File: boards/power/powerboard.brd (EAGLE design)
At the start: 83 x 42 mm, 42 parts, among them IC1 TPS5420, IC2 TPS5420

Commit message: finished powerboard changes
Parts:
- moved R4 11.2 mm to (43.5, 36.2)
- moved R1 7.13 mm to (33.6, 38.2)
- moved R7 3.36 mm to (39.5, 36.2), turned to 180 degrees
- moved R2 1.55 mm to (6.17, 8.89)
- moved U$1 1.52 mm to (51.8, 33.4)
- moved R3 1.05 mm to (5.48, 17.4)
- moved R6 1.05 mm to (5.56, 13.2)
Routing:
- net 5V: track 23.2 -> 35.5 mm
- net N$6: track 27.0 -> 34.5 mm
- net GND: track 0.37 -> 7.49 mm, vias 5 -> 6
- net N$5: track 2.56 -> 9.58 mm
- net N$12: track 30.5 -> 24.7 mm, vias 3 -> 2
- net N$19: track 1.16 -> 2.76 mm
- net N$18: track 5.03 -> 4.28 mm

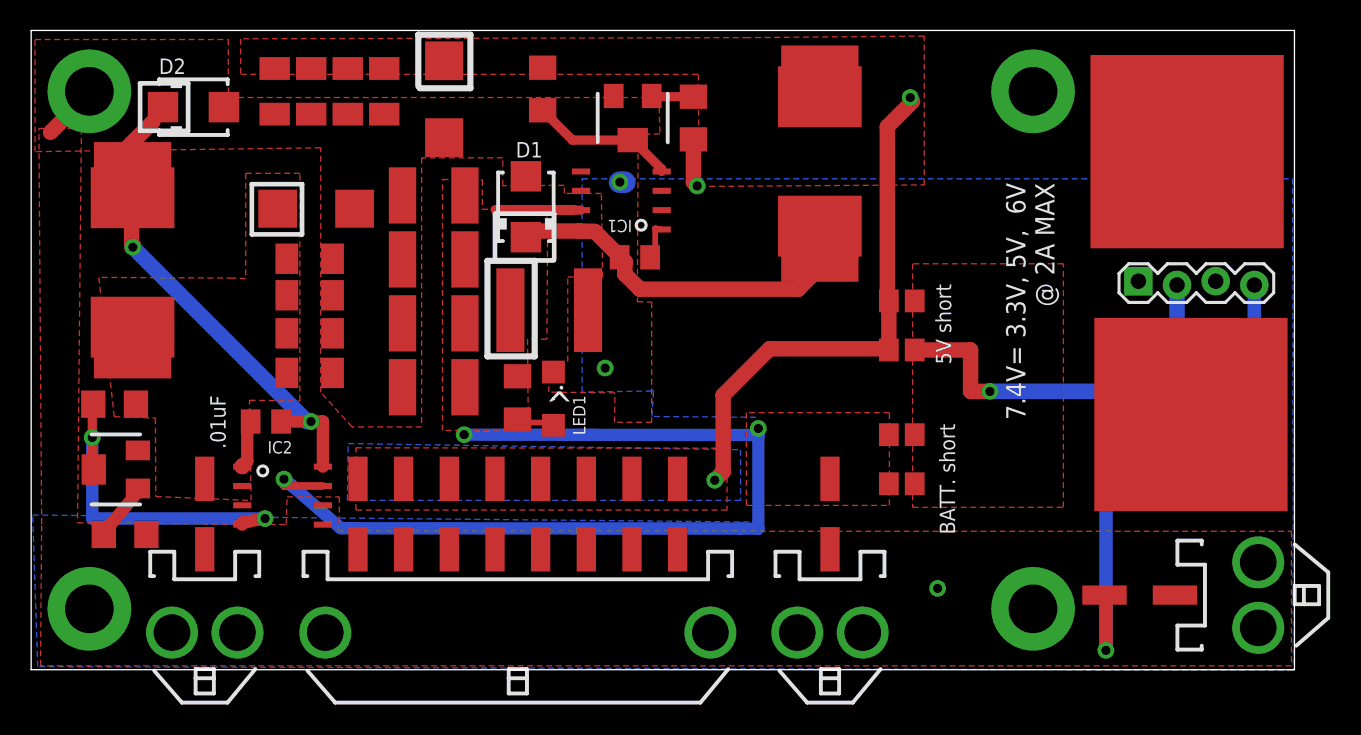
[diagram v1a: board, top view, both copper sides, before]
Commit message: changed resistors and fixed text
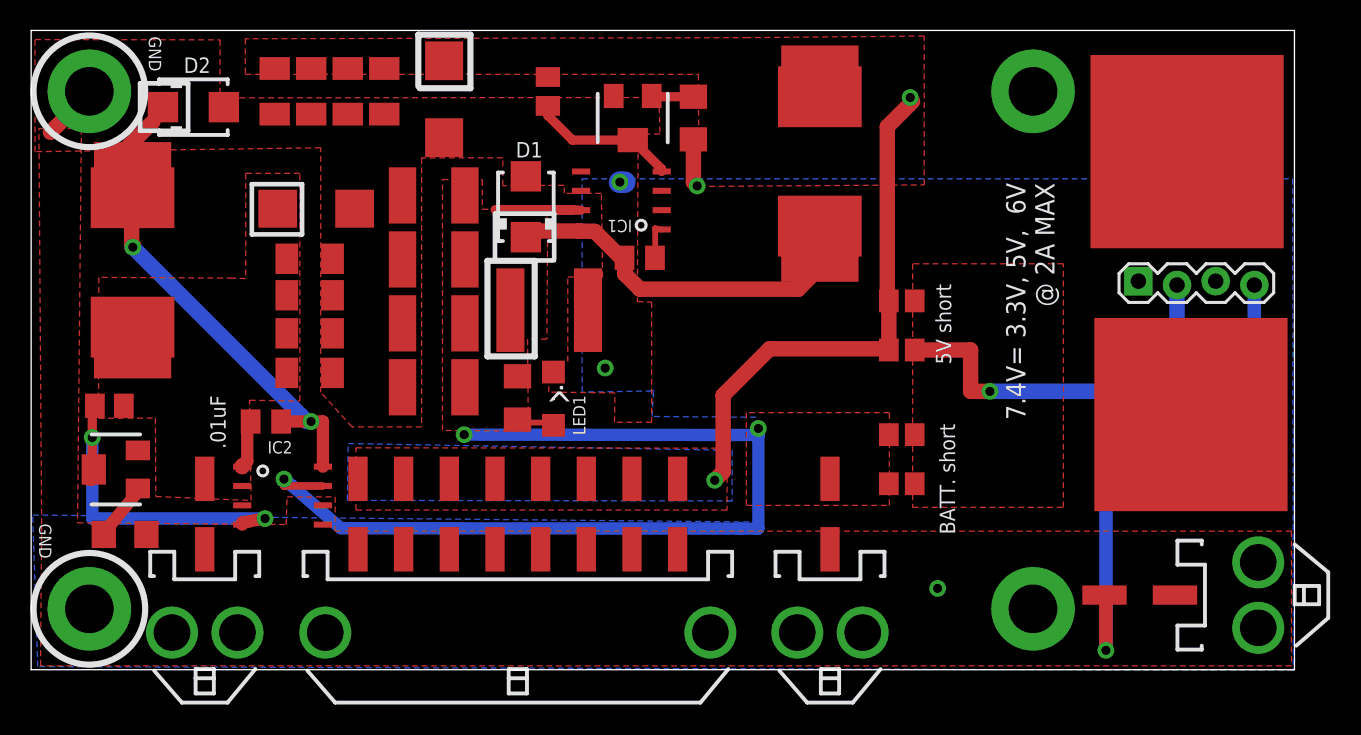
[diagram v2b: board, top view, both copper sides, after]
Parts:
- removed R1, R3: 10.0k, rcl:R3216
- added R12, R13: 10k, rcl:M0805
- R2, R4: value 500 -> 470
- moved C8 0.32 mm to (40.0, 27.1)
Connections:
- net 3_3V: now also R13.2; no longer R3.2
- net 5V: now also R12.2; no longer R1.2
- net N$12: now also R13.1; no longer R3.1
- net N$5: now also R12.1; no longer R1.1
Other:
- board text added: "GND"
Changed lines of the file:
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@@
 <setting verticaltext="up"/>
 </settings>
-<grid distance="0.01" unitdist="inch" unit="inch" style="lines" multiple="65" display="yes" altdistance="0.025" altunitdist="inch" altunit="inch"/>
+<grid distance="0.01" unitdist="mm" unit="mm" style="lines" multiple="65" display="yes" altdistance="0.025" altunitdist="inch" altunit="inch"/>
 <layers>
 <layer number="1" name="Top" color="4" fill="1" visible="yes" active="yes"/>
@@
 <text x="60.706" y="8.89" size="1.016" layer="25" font="vector" rot="R90">BATT. short</text>
 <text x="33.782" y="16.51" size="1.778" layer="25">^</text>
+<circle x="3.8246" y="4" radius="3.668" width="0.4064" layer="21"/>
+<text x="0.52" y="9.6" size="0.8128" layer="21" rot="SR270">GND</text>
+<text x="7.73" y="41.61" size="0.8128" layer="21" rot="SR270">GND</text>
+<circle x="3.8246" y="38" radius="3.668" width="0.4064" layer="21"/>
 </plain>
 <attributes>
@@
 <attribute name="NAME" x="33.6002" y="34.6696" size="1.016" layer="25" ratio="10" rot="R180"/>
 </element>
-<element name="C8" library="rcl" package="C0805K" value=".01uF" x="39.6642" y="27.094" smashed="yes">
-<attribute name="VALUE" x="38.9182" y="24.94" size="1.016" layer="27"/>
-</element>
-<element name="R1" library="rcl" package="R3216" value="10.0k" x="33.6074" y="38.154" smashed="yes" rot="R90">
-<attribute name="VALUE" x="35.8934" y="35.995" size="1.016" layer="27" rot="R90"/>
+<element name="C8" library="rcl" package="C0805K" value=".01uF" x="39.9842" y="27.064" smashed="yes">
+<attribute name="VALUE" x="39.2382" y="24.91" size="1.016" layer="27"/>
 </element>
 <element name="U$1" library="inductor-coilcraft-3" package="MSS1260" value="33uH" x="51.8188" y="33.3946" smashed="yes" rot="R180">
@@
 </element>
 <element name="D2" library="diode" package="SMA" value="MBRA340T3" x="10.662" y="36.9598" smashed="yes">
-<attribute name="NAME" x="8.3946" y="39.1376" size="1.016" layer="25" ratio="10"/>
+<attribute name="NAME" x="10.0246" y="39.2076" size="1.016" layer="25" ratio="10"/>
 </element>
 <element name="C17" library="rcl" package="C0805K" value=".01uF" x="15.4222" y="16.3056" smashed="yes" rot="R180">
 <attribute name="VALUE" x="11.7664" y="18.0224" size="1.016" layer="25" rot="R270"/>
-</element>
-<element name="R3" library="rcl" package="R3216" value="10.0k" x="5.4844" y="17.445" smashed="yes">
-<attribute name="VALUE" x="2.621" y="15.2634" size="1.016" layer="27" rot="R90"/>
 </element>
 <element name="U$3" library="inductor-coilcraft-3" package="MSS1260" value="33uH" x="6.6634" y="26.7566" smashed="yes">
@@
 <attribute name="VALUE" x="35.6624" y="38.5008" size="1.27" layer="27" rot="R270"/>
 </element>
-<element name="R2" library="rcl" package="R3216" value="500" x="6.1722" y="8.89" smashed="yes" rot="R180">
-<attribute name="VALUE" x="2.286" y="9.8552" size="1.016" layer="27" rot="R270"/>
-</element>
-<element name="R4" library="rcl" package="R3216" value="500" x="43.5102" y="36.2458" smashed="yes" rot="R90">
+<element name="R2" library="rcl" package="R3216" value="470" x="6.1722" y="8.89" smashed="yes" rot="R180">
+<attribute name="VALUE" x="2.226" y="10.5152" size="1.016" layer="27" rot="R270"/>
+</element>
+<element name="R4" library="rcl" package="R3216" value="470" x="43.5102" y="36.2458" smashed="yes" rot="R90">
 <attribute name="VALUE" x="44.9072" y="39.9542" size="1.016" layer="27" rot="R180"/>
 </element>
@@
 <attribute name="VALUE" x="31.236" y="19.647" size="1.016" layer="27"/>
 </element>
+<element name="R12" library="rcl" package="M0805" value="10k" x="33.95" y="37.99" smashed="yes" rot="R90">
+<attribute name="VALUE" x="32.43" y="36.18" size="1.27" layer="27" rot="R90"/>
+</element>
+<element name="R13" library="rcl" package="M0805" value="10k" x="5.14" y="17.34" smashed="yes">
+<attribute name="VALUE" x="7.27" y="16.79" size="1.27" layer="27"/>
+</element>
 </elements>
 <signals>
 <signal name="5V" class="1">
-<contactref element="R1" pad="2"/>
 <contactref element="C5" pad="1"/>
 <contactref element="C4" pad="1"/>
@@
 <polygon width="0.508" layer="1" isolate="0.8128">
 <vertex x="47.117" y="41.529"/>
-<vertex x="13.7668" y="41.4528"/>
-<vertex x="13.7668" y="39.116"/>
+<vertex x="14.0668" y="41.4528"/>
+<vertex x="14.0668" y="39.116"/>
 <vertex x="43.8404" y="39.116"/>
 <vertex x="43.8404" y="37.4142"/>
@@
 <vertex x="20.7746" y="11.1252"/>
 <vertex x="20.828" y="14.859"/>
-<vertex x="46.609" y="14.4526"/>
-<vertex x="46.609" y="11.1252"/>
+<vertex x="46.059" y="14.4126"/>
+<vertex x="46.059" y="11.0852"/>
 </polygon>
 <contactref element="X1" pad="P$9"/>
@@
 <wire x1="56.3508" y1="21.0058" x2="56.3118" y2="21.0058" width="1.016" layer="1"/>
 <wire x1="56.3118" y1="21.0058" x2="56.261" y2="20.955" width="1.016" layer="1"/>
+<contactref element="R12" pad="2"/>
 </signal>
 <signal name="N$2">
@@
 <wire x1="41" y1="27" x2="41" y2="29" width="0.381" layer="1"/>
 <wire x1="41" y1="29" x2="41.428" y2="28.924" width="0.381" layer="1"/>
-<wire x1="41" y1="27" x2="40.6642" y2="27.094" width="0.381" layer="1"/>
+<wire x1="41" y1="27" x2="40.9842" y2="27.064" width="0.381" layer="1"/>
 </signal>
 <signal name="N$5">
-<contactref element="R1" pad="1"/>
 <contactref element="IC1" pad="4"/>
 <contactref element="R7" pad="2"/>
-<wire x1="33.6074" y1="36.754" x2="35.5656" y2="34.7958" width="0.6096" layer="1"/>
 <wire x1="35.5656" y1="34.7958" x2="39.5224" y2="34.7958" width="0.6096" layer="1"/>
 <wire x1="39.5224" y1="34.7958" x2="41.428" y2="32.8902" width="0.6096" layer="1"/>
 <wire x1="41.428" y1="32.8902" x2="41.428" y2="32.734" width="0.6096" layer="1"/>
+<contactref element="R12" pad="1"/>
+<wire x1="35.5656" y1="34.7958" x2="33.95" y2="36.4114" width="0.6096" layer="1"/>
+<wire x1="33.95" y1="36.4114" x2="33.95" y2="37.04" width="0.6096" layer="1"/>
 </signal>
 <signal name="GND" class="1">
@@
 <vertex x="0.254" y="34.036"/>
 <vertex x="0.254" y="41.402"/>
-<vertex x="12.954" y="41.402"/>
-<vertex x="12.954" y="37.592"/>
+<vertex x="12.414" y="41.382"/>
+<vertex x="12.414" y="37.572"/>
 <vertex x="41.2412" y="37.592"/>
 <vertex x="41.3174" y="35.2044"/>
@@
 <vertex x="16.7522" y="9.5386"/>
 <vertex x="16.8148" y="11.3538"/>
-<vertex x="20.2438" y="11.3538"/>
-<vertex x="20.2438" y="9.9822"/>
-<vertex x="20.1168" y="9.0932"/>
-<vertex x="82.804" y="9.0932"/>
+<vertex x="19.9738" y="11.3538"/>
+<vertex x="19.9738" y="9.1032"/>
+<vertex x="82.804" y="9.1032"/>
 </polygon>
 <contactref element="LED1" pad="C"/>
@@
 <wire x1="40" y1="25" x2="39" y2="26" width="1.016" layer="1"/>
 <wire x1="50.4" y1="25" x2="40" y2="25" width="1.016" layer="1"/>
-<wire x1="39.0254" y1="26.7968" x2="38.6642" y2="27.094" width="0.381" layer="1"/>
+<wire x1="39.0254" y1="26.7968" x2="38.9842" y2="27.064" width="0.381" layer="1"/>
 <wire x1="49.631965625" y1="28.23630625" x2="51.8188" y2="29.1446" width="0.381" layer="1"/>
 <wire x1="50.4" y1="25" x2="52.832" y2="27.432" width="1.016" layer="1"/>
@@
 </signal>
 <signal name="3_3V" class="1">
-<contactref element="R3" pad="2"/>
 <contactref element="C14" pad="1"/>
 <contactref element="C13" pad="1"/>
@@
 <contactref element="X2" pad="P$2"/>
 <polygon width="0.508" layer="1">
-<vertex x="5.461" y="16.6174"/>
+<vertex x="4.431" y="16.5174"/>
 <vertex x="8.163" y="16.5354"/>
 <vertex x="8.1884" y="11.3782"/>
@@
 <vertex x="4.445" y="25.7744"/>
 </polygon>
+<contactref element="R13" pad="2"/>
 </signal>
 <signal name="N$10">
@@
 </signal>
 <signal name="N$12">
-<contactref element="R3" pad="1"/>
 <contactref element="IC2" pad="4"/>
 <contactref element="R6" pad="2"/>
 <wire x1="4.016" y1="13.254" x2="4.016" y2="15.254" width="0.6096" layer="1"/>
 <wire x1="4.016" y1="15.254" x2="4.016" y2="17.254" width="0.6096" layer="1"/>
-<wire x1="4.016" y1="17.254" x2="4.0844" y2="17.445" width="0.381" layer="1"/>
 <wire x1="4.016" y1="13.254" x2="4.1126" y2="13.1572" width="0.381" layer="1"/>
 <wire x1="4.1148" y1="13.1064" x2="4.1148" y2="12.8016" width="0.8128" layer="1"/>
@@
 <wire x1="13.8688" y1="9.5304" x2="13.8688" y2="9.6774" width="0.8128" layer="1"/>
 <wire x1="13.8688" y1="9.6774" x2="15.367" y2="9.9314" width="0.8128" layer="1"/>
+<contactref element="R13" pad="1"/>
+<wire x1="4.05" y1="17.254" x2="4.136" y2="17.34" width="0.6096" layer="1"/>
+<wire x1="4.136" y1="17.34" x2="4.19" y2="17.34" width="0.6096" layer="1"/>
+<wire x1="4.05" y1="17.254" x2="4.016" y2="17.254" width="0.6096" layer="1"/>
 </signal>
 <signal name="N$13">
